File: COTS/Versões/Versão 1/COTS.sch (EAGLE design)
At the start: 10 parts

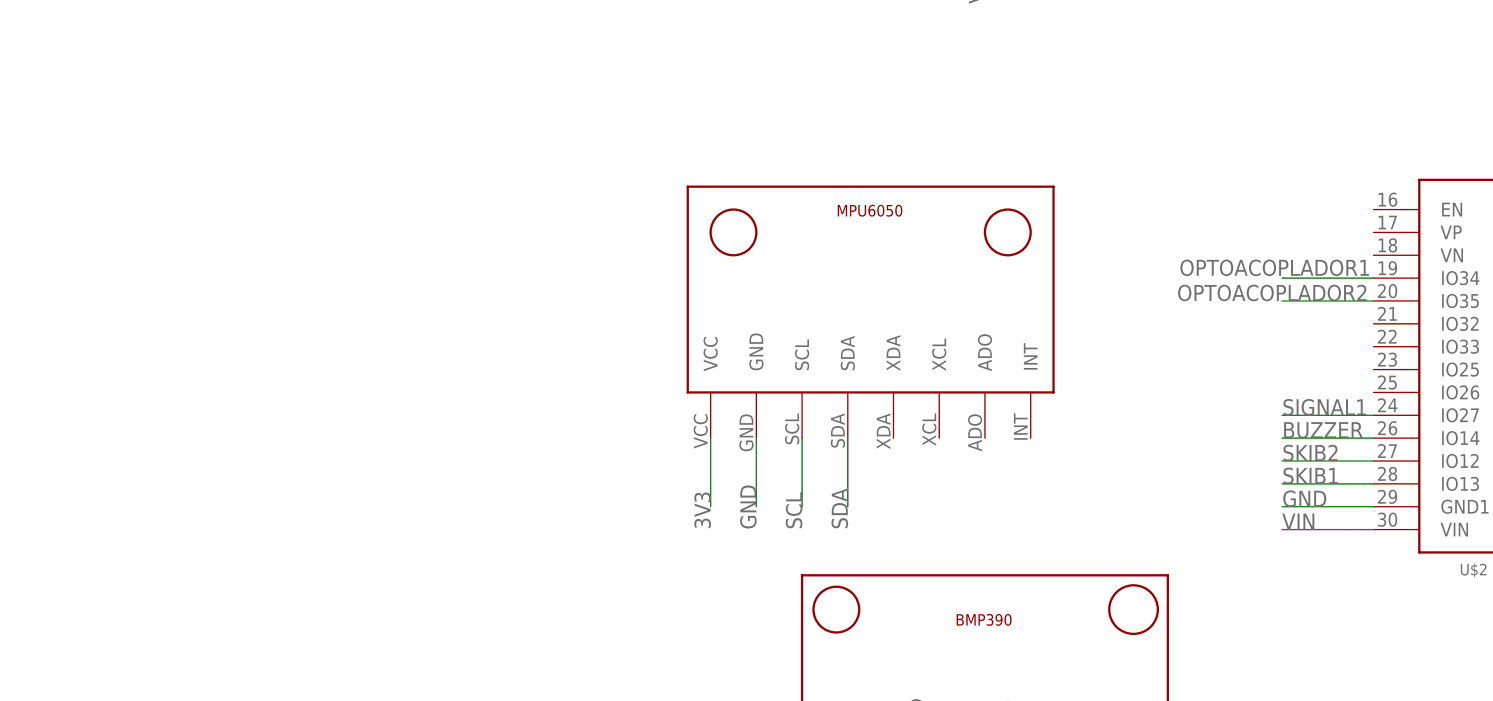
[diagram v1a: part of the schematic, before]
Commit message: FEAT: adicionando regulador de tensao 5V
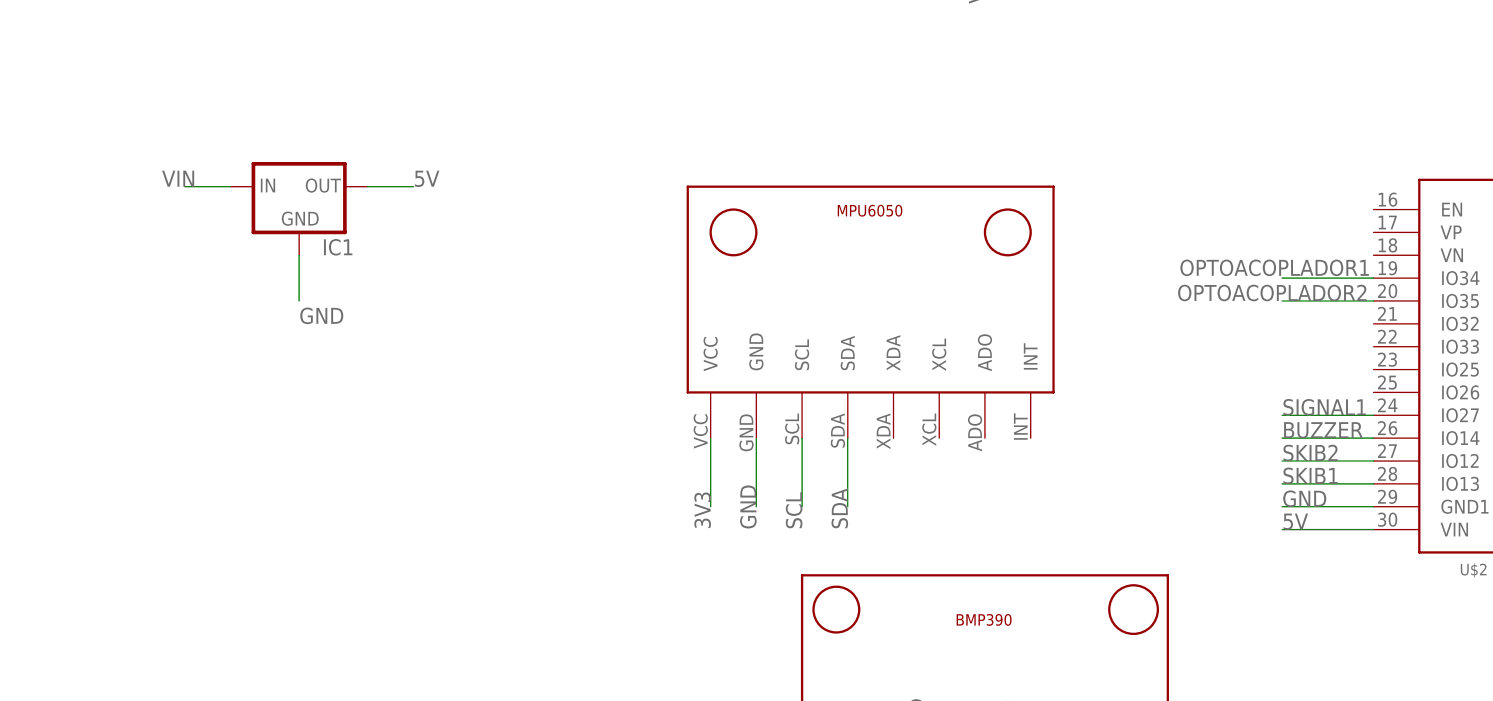
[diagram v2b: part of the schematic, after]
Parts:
- added IC1: (no value), v-reg:78XXL
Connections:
- new net 5V: IC1.OUT, U$2.VIN
- net GND: now also IC1.GND
- net VIN: now also IC1.IN; no longer U$2.VIN
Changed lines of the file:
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@@
 <part name="U$10" library="CRD" library_urn="urn:adsk.eagle:library:39051337" deviceset="PRESSION_BUTTON" device="" package3d_urn="urn:adsk.eagle:package:43483815/3" override_package3d_urn="urn:adsk.eagle:package:49474180/2" override_package_urn="urn:adsk.eagle:footprint:43483813/3"/>
 <part name="SP2" library="buzzer" library_urn="urn:adsk.eagle:library:113" deviceset="AL11P" device="" package3d_urn="urn:adsk.eagle:package:5308/1" override_package3d_urn="urn:adsk.eagle:package:49473303/2" override_package_urn="urn:adsk.eagle:footprint:5250/1"/>
+<part name="IC1" library="v-reg" library_urn="urn:adsk.eagle:library:409" deviceset="78XXL" device="" package3d_urn="urn:adsk.eagle:package:30361/1"/>
 </parts>
 <sheets>
@@
 <attribute name="VALUE" x="232.41" y="50.165" size="1.778" layer="96"/>
 </instance>
+<instance part="IC1" gate="A" x="-35.56" y="68.58" smashed="yes">
+<attribute name="NAME" x="-33.02" y="60.96" size="1.778" layer="95"/>
+<attribute name="VALUE" x="-33.02" y="58.42" size="1.778" layer="96"/>
+</instance>
 </instances>
 <busses>
@@
 <net name="VIN" class="0">
 <segment>
-<pinref part="U$2" gate="G$1" pin="VIN"/>
-<wire x1="83.82" y1="30.48" x2="73.66" y2="30.48" width="0.1524" layer="91"/>
-<label x="73.66" y="30.48" size="1.778" layer="95"/>
-</segment>
-<segment>
 <wire x1="154.94" y1="50.8" x2="154.94" y2="43.18" width="0.1524" layer="91"/>
 <label x="154.94" y="38.1" size="1.778" layer="95" rot="R90"/>
@@
 <label x="182.88" y="78.74" size="1.778" layer="95" rot="R90"/>
 </segment>
+<segment>
+<pinref part="IC1" gate="A" pin="IN"/>
+<wire x1="-43.18" y1="68.58" x2="-48.26" y2="68.58" width="0.1524" layer="91"/>
+<label x="-50.8" y="68.58" size="1.778" layer="95"/>
+</segment>
 </net>
 <net name="GND" class="0">
@@
 <label x="228.6" y="43.18" size="1.778" layer="95"/>
 </segment>
+<segment>
+<pinref part="IC1" gate="A" pin="GND"/>
+<wire x1="-35.56" y1="60.96" x2="-35.56" y2="55.88" width="0.1524" layer="91"/>
+<label x="-35.56" y="53.34" size="1.778" layer="95"/>
+</segment>
 </net>
 <net name="SKIB1" class="0">
@@
 </segment>
 </net>
+<net name="5V" class="0">
+<segment>
+<pinref part="IC1" gate="A" pin="OUT"/>
+<wire x1="-27.94" y1="68.58" x2="-22.86" y2="68.58" width="0.1524" layer="91"/>
+<label x="-22.86" y="68.58" size="1.778" layer="95"/>
+</segment>
+<segment>
+<pinref part="U$2" gate="G$1" pin="VIN"/>
+<wire x1="83.82" y1="30.48" x2="73.66" y2="30.48" width="0.1524" layer="91"/>
+<label x="73.66" y="30.48" size="1.778" layer="95"/>
+</segment>
+</net>

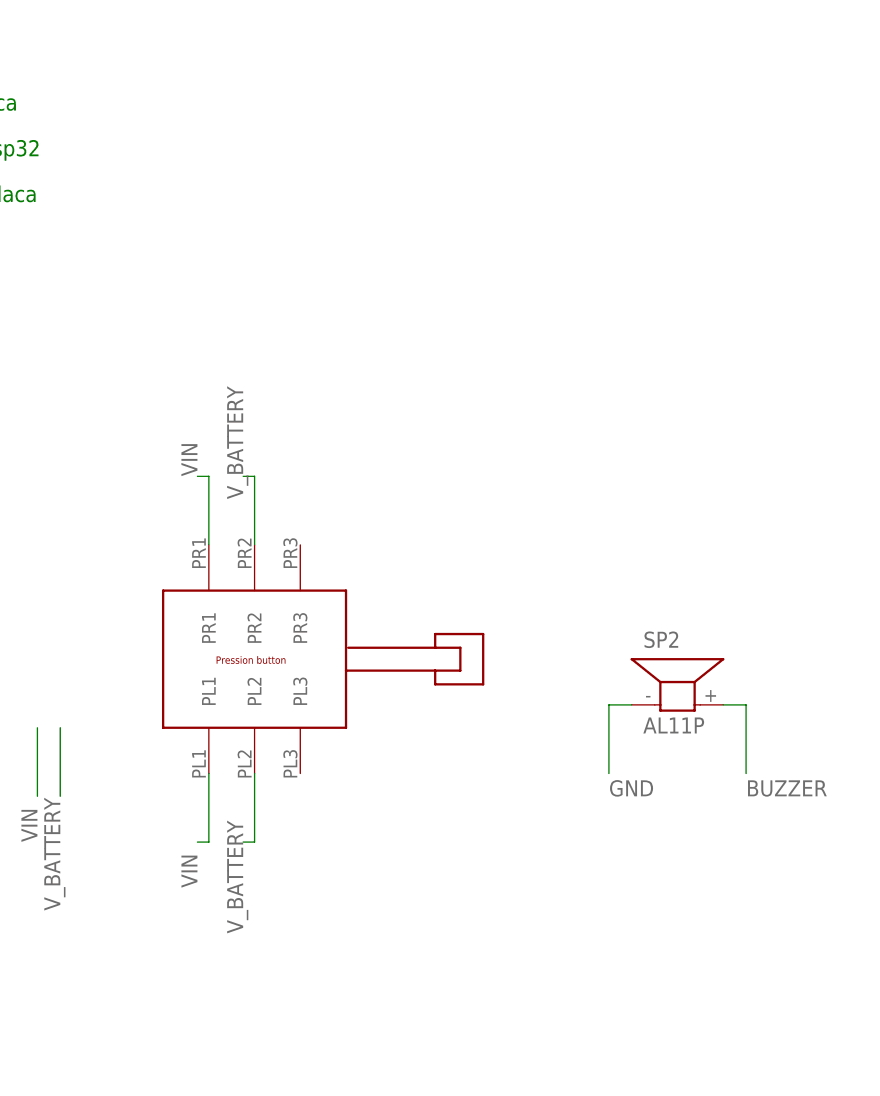
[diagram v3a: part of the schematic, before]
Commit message: FIX: consertando chave de acionamento
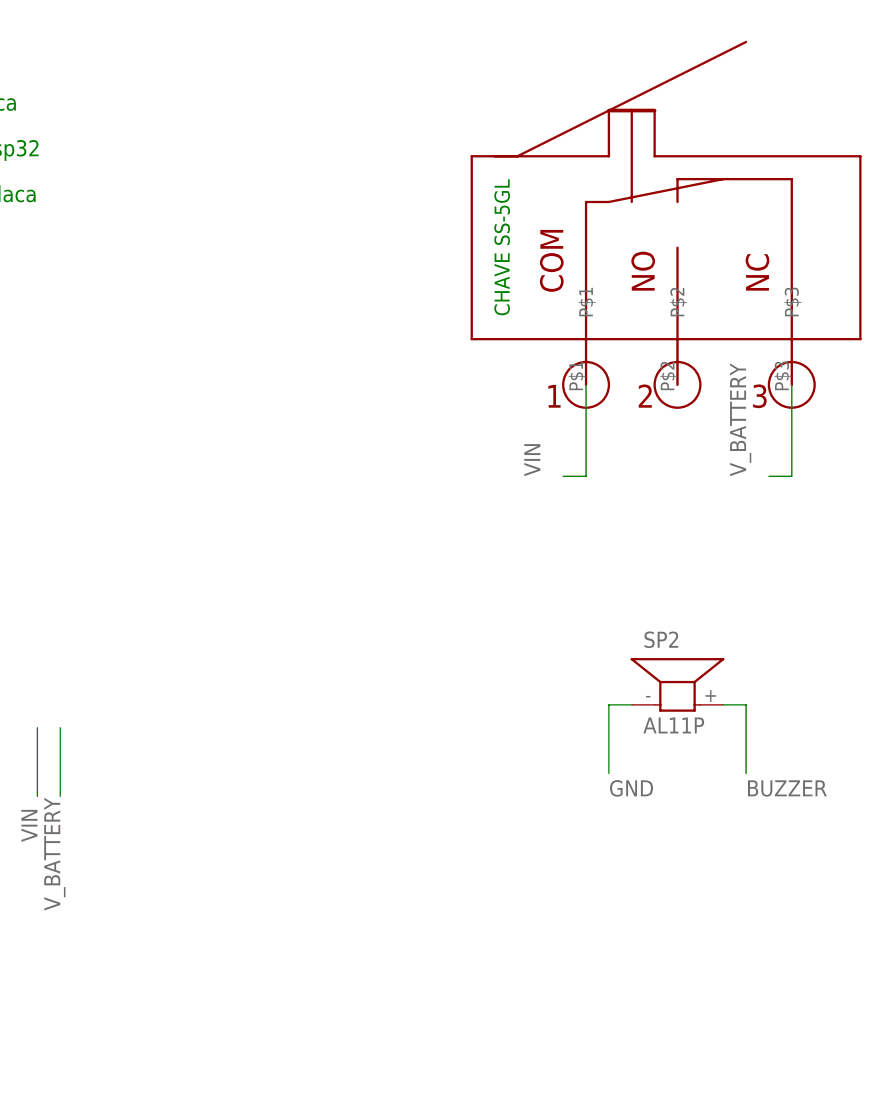
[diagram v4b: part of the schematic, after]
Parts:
- removed U$10: PRESSION_BUTTON, CRD:PRESSION_BUTTON
- added U$8: CHAVE_SS-5GL, CRD:CHAVE_SS-5GL
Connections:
- net VIN: now also U$8.P$1; no longer U$10.PL1, U$10.PR1
- net V_BATTERY: now also U$8.P$3; no longer U$10.PL2, U$10.PR2
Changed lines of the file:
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@@
 <part name="U$7" library="CRD" library_urn="urn:adsk.eagle:library:39051337" deviceset="JST2.54X2P" device="" package3d_urn="urn:adsk.eagle:package:39191967/2"/>
 <part name="U$9" library="CRD" library_urn="urn:adsk.eagle:library:39051337" deviceset="JST2.54X2P" device="" package3d_urn="urn:adsk.eagle:package:39191967/2"/>
-<part name="U$10" library="CRD" library_urn="urn:adsk.eagle:library:39051337" deviceset="PRESSION_BUTTON" device="" package3d_urn="urn:adsk.eagle:package:43483815/3" override_package3d_urn="urn:adsk.eagle:package:49474180/2" override_package_urn="urn:adsk.eagle:footprint:43483813/3"/>
-<part name="SP2" library="buzzer" library_urn="urn:adsk.eagle:library:113" deviceset="AL11P" device="" package3d_urn="urn:adsk.eagle:package:5308/1" override_package3d_urn="urn:adsk.eagle:package:49473303/2" override_package_urn="urn:adsk.eagle:footprint:5250/1"/>
-<part name="IC1" library="v-reg" library_urn="urn:adsk.eagle:library:409" deviceset="78XXL" device="" package3d_urn="urn:adsk.eagle:package:30361/1" override_package3d_urn="urn:adsk.eagle:package:49478860/2" override_package_urn="urn:adsk.eagle:footprint:30303/1"/>
+<part name="SP2" library="buzzer" library_urn="urn:adsk.eagle:library:113" deviceset="AL11P" device="" package3d_urn="urn:adsk.eagle:package:5308/1" override_package3d_urn="urn:adsk.eagle:package:49481862/2" override_package_urn="urn:adsk.eagle:footprint:5250/1"/>
+<part name="IC1" library="v-reg" library_urn="urn:adsk.eagle:library:409" deviceset="78XXL" device="" package3d_urn="urn:adsk.eagle:package:30361/1" override_package3d_urn="urn:adsk.eagle:package:49481863/2" override_package_urn="urn:adsk.eagle:footprint:30303/1"/>
+<part name="U$8" library="CRD" library_urn="urn:adsk.eagle:library:39051337" deviceset="CHAVE_SS-5GL" device="" package3d_urn="urn:adsk.eagle:package:45208058/14"/>
 </parts>
 <sheets>
@@
 <instance part="U$7" gate="G$1" x="60.96" y="116.84" smashed="yes"/>
 <instance part="U$9" gate="G$1" x="-73.66" y="116.84" smashed="yes"/>
-<instance part="U$10" gate="G$1" x="195.58" y="58.42" smashed="yes"/>
 <instance part="SP2" gate="G$1" x="236.22" y="53.34" smashed="yes">
 <attribute name="NAME" x="232.41" y="59.69" size="1.778" layer="95"/>
@@
 <attribute name="VALUE" x="-33.02" y="58.42" size="1.778" layer="96"/>
 </instance>
+<instance part="U$8" gate="G$1" x="236.22" y="101.6" smashed="yes"/>
 </instances>
 <busses>
@@
 </segment>
 <segment>
-<pinref part="U$10" gate="G$1" pin="PL1"/>
-<wire x1="184.15" y1="45.72" x2="184.15" y2="38.1" width="0.1524" layer="91"/>
-<wire x1="184.15" y1="38.1" x2="182.88" y2="38.1" width="0.1524" layer="91"/>
-<label x="182.88" y="33.02" size="1.778" layer="95" rot="R90"/>
-</segment>
-<segment>
-<pinref part="U$10" gate="G$1" pin="PR1"/>
-<wire x1="184.15" y1="71.12" x2="184.15" y2="78.74" width="0.1524" layer="91"/>
-<wire x1="184.15" y1="78.74" x2="182.88" y2="78.74" width="0.1524" layer="91"/>
-<label x="182.88" y="78.74" size="1.778" layer="95" rot="R90"/>
-</segment>
-<segment>
 <pinref part="IC1" gate="A" pin="IN"/>
 <wire x1="-43.18" y1="68.58" x2="-48.26" y2="68.58" width="0.1524" layer="91"/>
 <label x="-50.8" y="68.58" size="1.778" layer="95"/>
+</segment>
+<segment>
+<pinref part="U$8" gate="G$1" pin="P$1"/>
+<wire x1="226.06" y1="88.9" x2="226.06" y2="78.74" width="0.1524" layer="91"/>
+<wire x1="226.06" y1="78.74" x2="223.52" y2="78.74" width="0.1524" layer="91"/>
+<label x="220.98" y="78.74" size="1.778" layer="95" rot="R90"/>
 </segment>
 </net>
@@
 </segment>
 <segment>
-<pinref part="U$10" gate="G$1" pin="PL2"/>
-<wire x1="189.23" y1="45.72" x2="189.23" y2="38.1" width="0.1524" layer="91"/>
-<wire x1="189.23" y1="38.1" x2="187.96" y2="38.1" width="0.1524" layer="91"/>
-<label x="187.96" y="27.94" size="1.778" layer="95" rot="R90"/>
-</segment>
-<segment>
-<pinref part="U$10" gate="G$1" pin="PR2"/>
-<wire x1="189.23" y1="71.12" x2="189.23" y2="78.74" width="0.1524" layer="91"/>
-<wire x1="189.23" y1="78.74" x2="187.96" y2="78.74" width="0.1524" layer="91"/>
-<label x="187.96" y="76.2" size="1.778" layer="95" rot="R90"/>
-</segment>
-</net>
+<pinref part="U$8" gate="G$1" pin="P$3"/>
+<wire x1="248.92" y1="88.9" x2="248.92" y2="78.74" width="0.1524" layer="91"/>
+<wire x1="248.92" y1="78.74" x2="246.38" y2="78.74" width="0.1524" layer="91"/>
+<label x="243.84" y="78.74" size="1.778" layer="95" rot="R90"/>
+</segment>
+</net>

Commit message: atualização placas
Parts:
- added U$10: BMP280V1, CRD:BMP280V1
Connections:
- net 3V3: now also U$10.VCC
- net GND: now also U$10.GND; no longer U$2.GND
- net SCL: now also U$10.SCL
- net SDA: now also U$10.SDA
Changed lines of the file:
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@@
 <drawing>
 <settings>
-<setting alwaysvectorfont="no"/>
+<setting alwaysvectorfont="yes"/>
 <setting verticaltext="up"/>
 </settings>
@@
 <part name="IC1" library="v-reg" library_urn="urn:adsk.eagle:library:409" deviceset="78XXL" device="" package3d_urn="urn:adsk.eagle:package:30361/1" override_package3d_urn="urn:adsk.eagle:package:49481863/2" override_package_urn="urn:adsk.eagle:footprint:30303/1"/>
 <part name="U$8" library="CRD" library_urn="urn:adsk.eagle:library:39051337" deviceset="CHAVE_SS-5GL" device="" package3d_urn="urn:adsk.eagle:package:45208058/14"/>
+<part name="U$10" library="CRD" library_urn="urn:adsk.eagle:library:39051337" deviceset="BMP280" device="V1" package3d_urn="urn:adsk.eagle:package:39029072/6"/>
 </parts>
 <sheets>
@@
 </instance>
 <instance part="U$8" gate="G$1" x="236.22" y="101.6" smashed="yes"/>
+<instance part="U$10" gate="G$1" x="88.9" y="5.08" smashed="yes"/>
 </instances>
 <busses>
@@
 </segment>
 <segment>
-<pinref part="U$2" gate="G$1" pin="GND"/>
-<wire x1="119.38" y1="33.02" x2="129.54" y2="33.02" width="0.1524" layer="91"/>
-<label x="129.54" y="33.02" size="1.778" layer="95"/>
-</segment>
-<segment>
 <pinref part="U$1" gate="G$1" pin="GND"/>
 <wire x1="15.24" y1="40.64" x2="15.24" y2="33.02" width="0.1524" layer="91"/>
@@
 <label x="-35.56" y="53.34" size="1.778" layer="95"/>
 </segment>
+<segment>
+<pinref part="U$10" gate="G$1" pin="GND"/>
+<wire x1="81.28" y1="-10.16" x2="81.28" y2="-17.78" width="0.1524" layer="91"/>
+<label x="81.28" y="-20.32" size="1.778" layer="95" rot="R90"/>
+</segment>
 </net>
 <net name="SKIB1" class="0">
@@
 <label x="48.26" y="-12.7" size="1.778" layer="95" rot="R90"/>
 </segment>
+<segment>
+<pinref part="U$10" gate="G$1" pin="SDA"/>
+<wire x1="91.44" y1="-10.16" x2="91.44" y2="-17.78" width="0.1524" layer="91"/>
+<label x="91.44" y="-20.32" size="1.778" layer="95" rot="R90"/>
+</segment>
 </net>
 <net name="SCL" class="0">
@@
 <label x="38.1" y="-12.7" size="1.778" layer="95" rot="R90"/>
 </segment>
+<segment>
+<pinref part="U$10" gate="G$1" pin="SCL"/>
+<wire x1="86.36" y1="-10.16" x2="86.36" y2="-17.78" width="0.1524" layer="91"/>
+<label x="86.36" y="-20.32" size="1.778" layer="95" rot="R90"/>
+</segment>
 </net>
 <net name="3V3" class="0">
@@
 <label x="10.16" y="93.98" size="1.778" layer="95" rot="R90"/>
 </segment>
-</net>
+<segment>
+<pinref part="U$10" gate="G$1" pin="VCC"/>
+<wire x1="76.2" y1="-10.16" x2="76.2" y2="-17.78" width="0.1524" layer="91"/>
+<label x="76.2" y="-20.32" size="1.778" layer="95" rot="R90"/>
+</segment>
+</net>
